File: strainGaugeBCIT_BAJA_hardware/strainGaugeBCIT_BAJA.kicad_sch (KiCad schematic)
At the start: 1 part

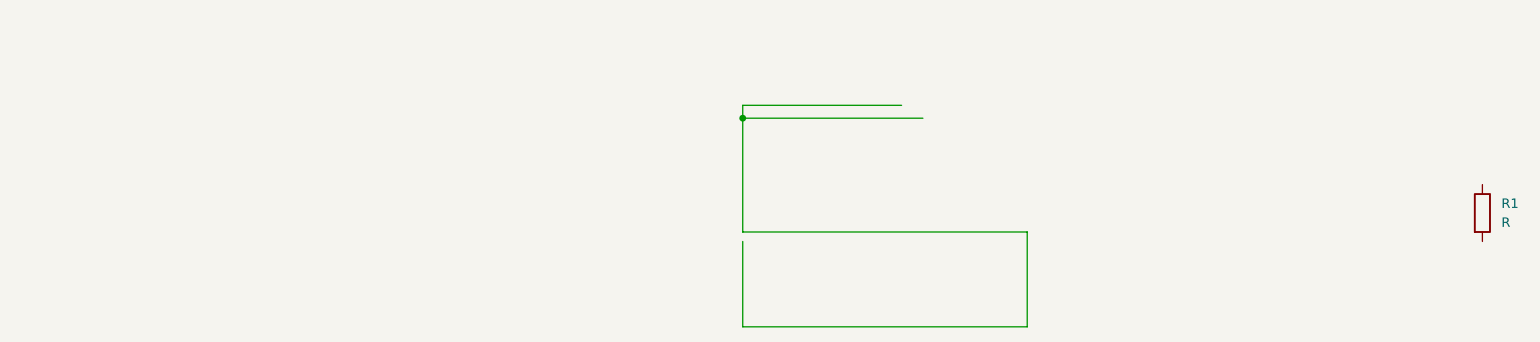
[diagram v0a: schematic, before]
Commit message: idea of how strain gauge interacts with MCU added. Not enough data to perform calculations
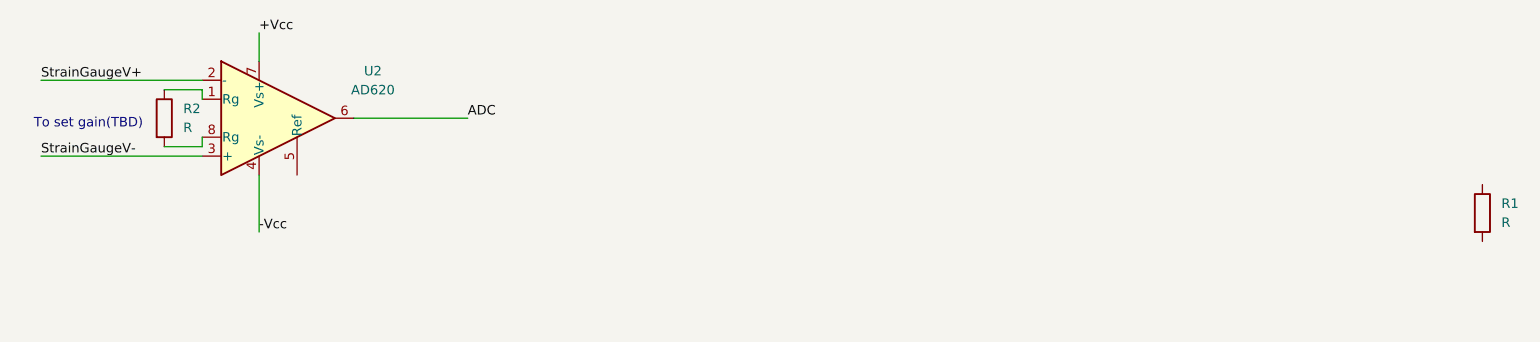
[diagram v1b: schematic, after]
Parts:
- added R2: R, symbol Device:R
- added U2: AD620, symbol Amplifier_Instrumentation:AD620
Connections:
- new net: R2.1, U2.1 (Rg)
- new net: R2.2, U2.8 (Rg)
- new net +Vcc: U2.7 (Vs+)
- new net -Vcc: U2.4 (Vs-)
- new net ADC: U2.6
- new net StrainGaugeV+: U2.2 (-)
- new net StrainGaugeV-: U2.3 (+)
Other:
- note added: "To set gain(TBD)"
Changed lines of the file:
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@@
 	(generator_version "8.0")
 	(paper "A4")
-	(junction
-		(at 124.46 77.47)
-		(diameter 0)
-		(color 0 0 0 0)
-	)
-	(wire
-		(pts
-			(xy 162.56 105.41) (xy 162.56 92.71)
-		)
-		(stroke
-			(width 0)
-			(type default)
-		)
-	)
-	(wire
-		(pts
-			(xy 124.46 93.98) (xy 124.46 105.41)
-		)
-		(stroke
-			(width 0)
-			(type default)
-		)
-	)
-	(wire
-		(pts
-			(xy 124.46 77.47) (xy 148.59 77.47)
-		)
-		(stroke
-			(width 0)
-			(type default)
-		)
-	)
-	(wire
-		(pts
-			(xy 124.46 105.41) (xy 162.56 105.41)
-		)
-		(stroke
-			(width 0)
-			(type default)
-		)
-	)
-	(wire
-		(pts
-			(xy 162.56 92.71) (xy 124.46 92.71)
-		)
-		(stroke
-			(width 0)
-			(type default)
-		)
-	)
-	(wire
-		(pts
-			(xy 124.46 75.7443) (xy 145.7364 75.7443)
-		)
-		(stroke
-			(width 0)
-			(type default)
-		)
-	)
-	(wire
-		(pts
-			(xy 124.46 77.47) (xy 124.46 92.71)
-		)
-		(stroke
-			(width 0)
-			(type default)
-		)
-	)
-	(wire
-		(pts
-			(xy 124.46 75.7443) (xy 124.46 77.47)
-		)
-		(stroke
-			(width 0)
-			(type default)
-		)
-	)
+	(wire
+		(pts
+			(xy 46.99 81.28) (xy 52.07 81.28)
+		)
+		(stroke
+			(width 0)
+			(type default)
+		)
+	)
+	(wire
+		(pts
+			(xy 72.39 77.47) (xy 87.63 77.47)
+		)
+		(stroke
+			(width 0)
+			(type default)
+		)
+	)
+	(wire
+		(pts
+			(xy 59.69 66.04) (xy 59.69 69.85)
+		)
+		(stroke
+			(width 0)
+			(type default)
+		)
+	)
+	(wire
+		(pts
+			(xy 52.07 74.93) (xy 52.07 73.66)
+		)
+		(stroke
+			(width 0)
+			(type default)
+		)
+	)
+	(wire
+		(pts
+			(xy 30.48 72.39) (xy 52.07 72.39)
+		)
+		(stroke
+			(width 0)
+			(type default)
+		)
+	)
+	(wire
+		(pts
+			(xy 52.07 81.28) (xy 52.07 80.01)
+		)
+		(stroke
+			(width 0)
+			(type default)
+		)
+	)
+	(wire
+		(pts
+			(xy 52.07 73.66) (xy 46.99 73.66)
+		)
+		(stroke
+			(width 0)
+			(type default)
+		)
+	)
+	(wire
+		(pts
+			(xy 30.48 82.55) (xy 52.07 82.55)
+		)
+		(stroke
+			(width 0)
+			(type default)
+		)
+	)
+	(wire
+		(pts
+			(xy 59.69 92.71) (xy 59.69 85.09)
+		)
+		(stroke
+			(width 0)
+			(type default)
+		)
+	)
+	(text "To set gain(TBD)"
+		(exclude_from_sim no)
+		(at 36.83 78.232 0)
+		(effects
+			(font
+				(size 1.27 1.27)
+			)
+		)
+	)
+	(label "+Vcc"
+		(at 59.69 66.04 0)
+		(fields_autoplaced yes)
+		(effects
+			(font
+				(size 1.27 1.27)
+			)
+			(justify left bottom)
+		)
+	)
+	(label "ADC"
+		(at 87.63 77.47 0)
+		(fields_autoplaced yes)
+		(effects
+			(font
+				(size 1.27 1.27)
+			)
+			(justify left bottom)
+		)
+	)
+	(label "StrainGaugeV-"
+		(at 30.48 82.55 0)
+		(fields_autoplaced yes)
+		(effects
+			(font
+				(size 1.27 1.27)
+			)
+			(justify left bottom)
+		)
+	)
+	(label "-Vcc"
+		(at 59.69 92.71 0)
+		(fields_autoplaced yes)
+		(effects
+			(font
+				(size 1.27 1.27)
+			)
+			(justify left bottom)
+		)
+	)
+	(label "StrainGaugeV+"
+		(at 30.48 72.39 0)
+		(fields_autoplaced yes)
+		(effects
+			(font
+				(size 1.27 1.27)
+			)
+			(justify left bottom)
+		)
+	)
+	(symbol
+		(lib_id "Amplifier_Instrumentation:AD620")
+		(at 62.23 77.47 0)
+		(unit 1)
+		(exclude_from_sim no)
+		(in_bom yes)
+		(on_board yes)
+		(dnp no)
+		(fields_autoplaced yes)
+		(property "Reference" "U2"
+			(at 74.93 71.1514 0)
+			(effects
+				(font
+					(size 1.27 1.27)
+				)
+			)
+		)
+		(property "Value" "AD620"
+			(at 74.93 73.6914 0)
+			(effects
+				(font
+					(size 1.27 1.27)
+				)
+			)
+		)
+		(property "Footprint" ""
+			(at 62.23 77.47 0)
+			(effects
+				(font
+					(size 1.27 1.27)
+				)
+				(hide yes)
+			)
+		)
+		(property "Datasheet" "https://www.analog.com/media/en/technical-documentation/data-sheets/AD620.pdf"
+			(at 62.23 77.47 0)
+			(effects
+				(font
+					(size 1.27 1.27)
+				)
+				(hide yes)
+			)
+		)
+		(property "Description" "Low Cost, Low Power, Instrumentation Amplifier, DIP-8/SOIC-8"
+			(at 62.23 77.47 0)
+			(effects
+				(font
+					(size 1.27 1.27)
+				)
+				(hide yes)
+			)
+		)
+		(pin "8"
+		)
+		(pin "4"
+		)
+		(pin "6"
+		)
+		(pin "1"
+		)
+		(pin "2"
+		)
+		(pin "3"
+		)
+		(pin "5"
+		)
+		(pin "7"
+		)
+		(instances
+			(project "strainGaugeBCIT_BAJA"
+				(path "/8162a86f-8c2b-4bf1-82ac-a8a91f9f1fb6"
+					(reference "U2")
+					(unit 1)
+				)
+			)
+		)
+	)
+	(symbol
+		(lib_id "Device:R")
+		(at 46.99 77.47 0)
+		(unit 1)
+		(exclude_from_sim no)
+		(in_bom yes)
+		(on_board yes)
+		(dnp no)
+		(fields_autoplaced yes)
+		(property "Reference" "R2"
+			(at 49.53 76.1999 0)
+			(effects
+				(font
+					(size 1.27 1.27)
+				)
+				(justify left)
+			)
+		)
+		(property "Value" "R"
+			(at 49.53 78.7399 0)
+			(effects
+				(font
+					(size 1.27 1.27)
+				)
+				(justify left)
+			)
+		)
+		(property "Footprint" ""
+			(at 45.212 77.47 90)
+			(effects
+				(font
+					(size 1.27 1.27)
+				)
+				(hide yes)
+			)
+		)
+		(property "Datasheet" "~"
+			(at 46.99 77.47 0)
+			(effects
+				(font
+					(size 1.27 1.27)
+				)
+				(hide yes)
+			)
+		)
+		(property "Description" "Resistor"
+			(at 46.99 77.47 0)
+			(effects
+				(font
+					(size 1.27 1.27)
+				)
+				(hide yes)
+			)
+		)
+		(pin "1"
+		)
+		(pin "2"
+		)
+		(instances
+			(project "strainGaugeBCIT_BAJA"
+				(path "/8162a86f-8c2b-4bf1-82ac-a8a91f9f1fb6"
+					(reference "R2")
+					(unit 1)
+				)
+			)
+		)
+	)
